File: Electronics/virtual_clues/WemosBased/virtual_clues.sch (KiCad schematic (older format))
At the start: 22 parts, among them Q1 IRLB8721PBF, U1 L7805

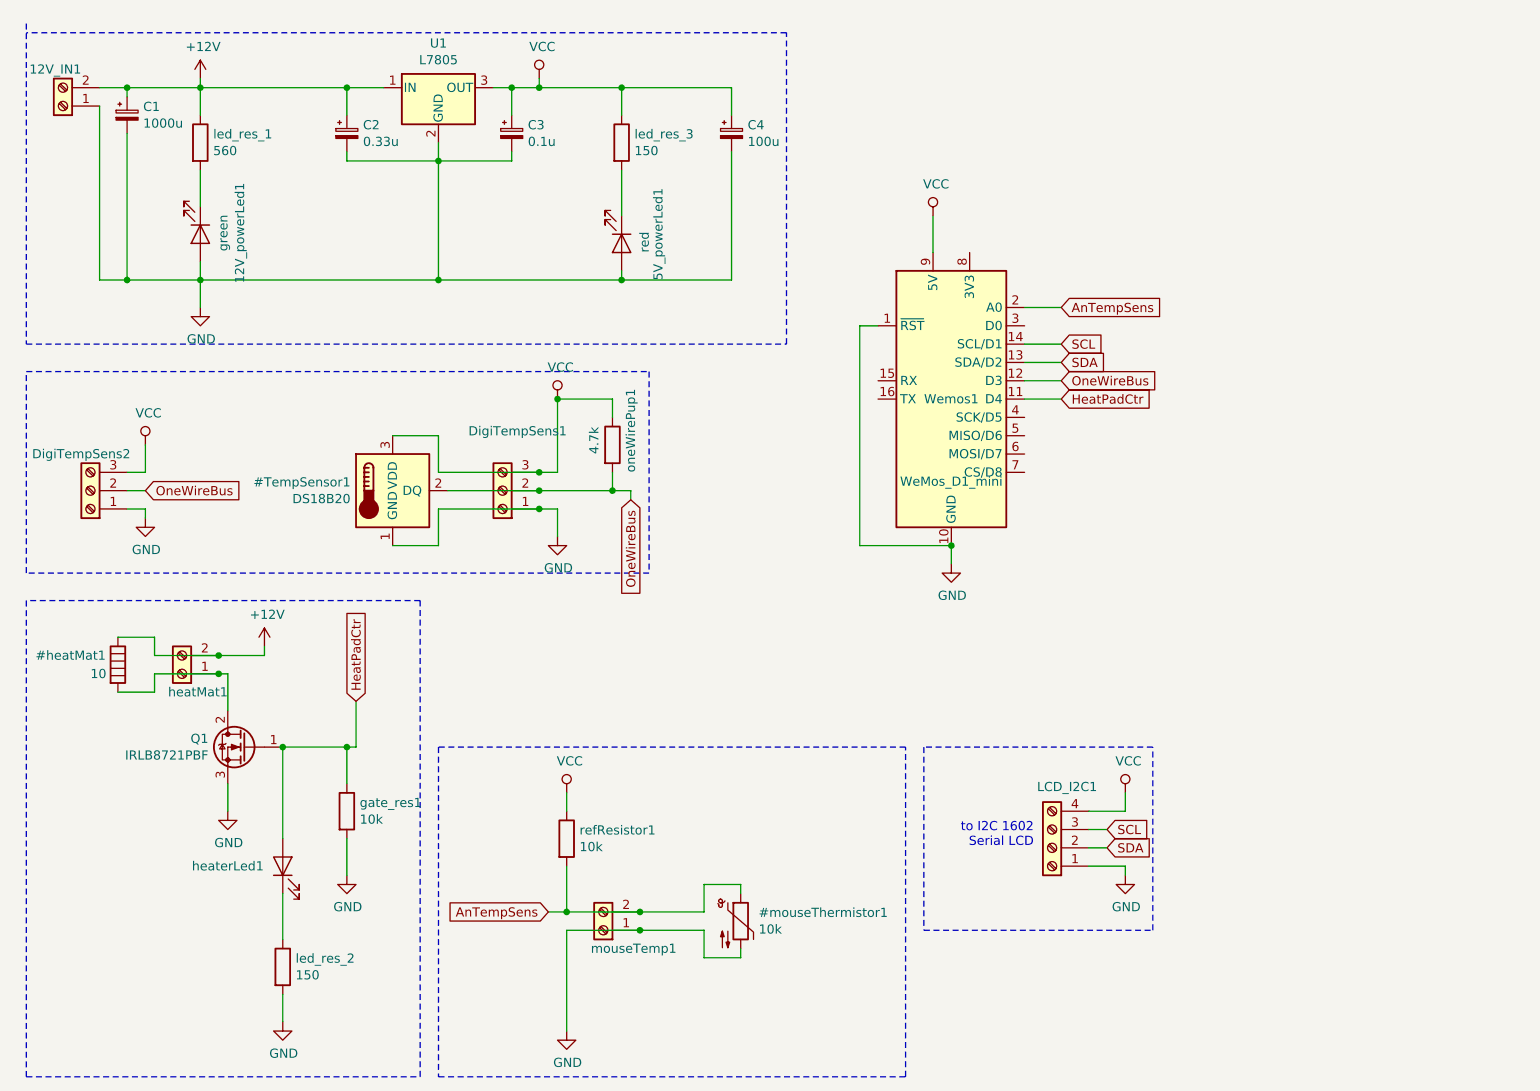
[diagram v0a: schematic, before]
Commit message: update PCB for 3rd temp sensor and additional heat pad + better labels
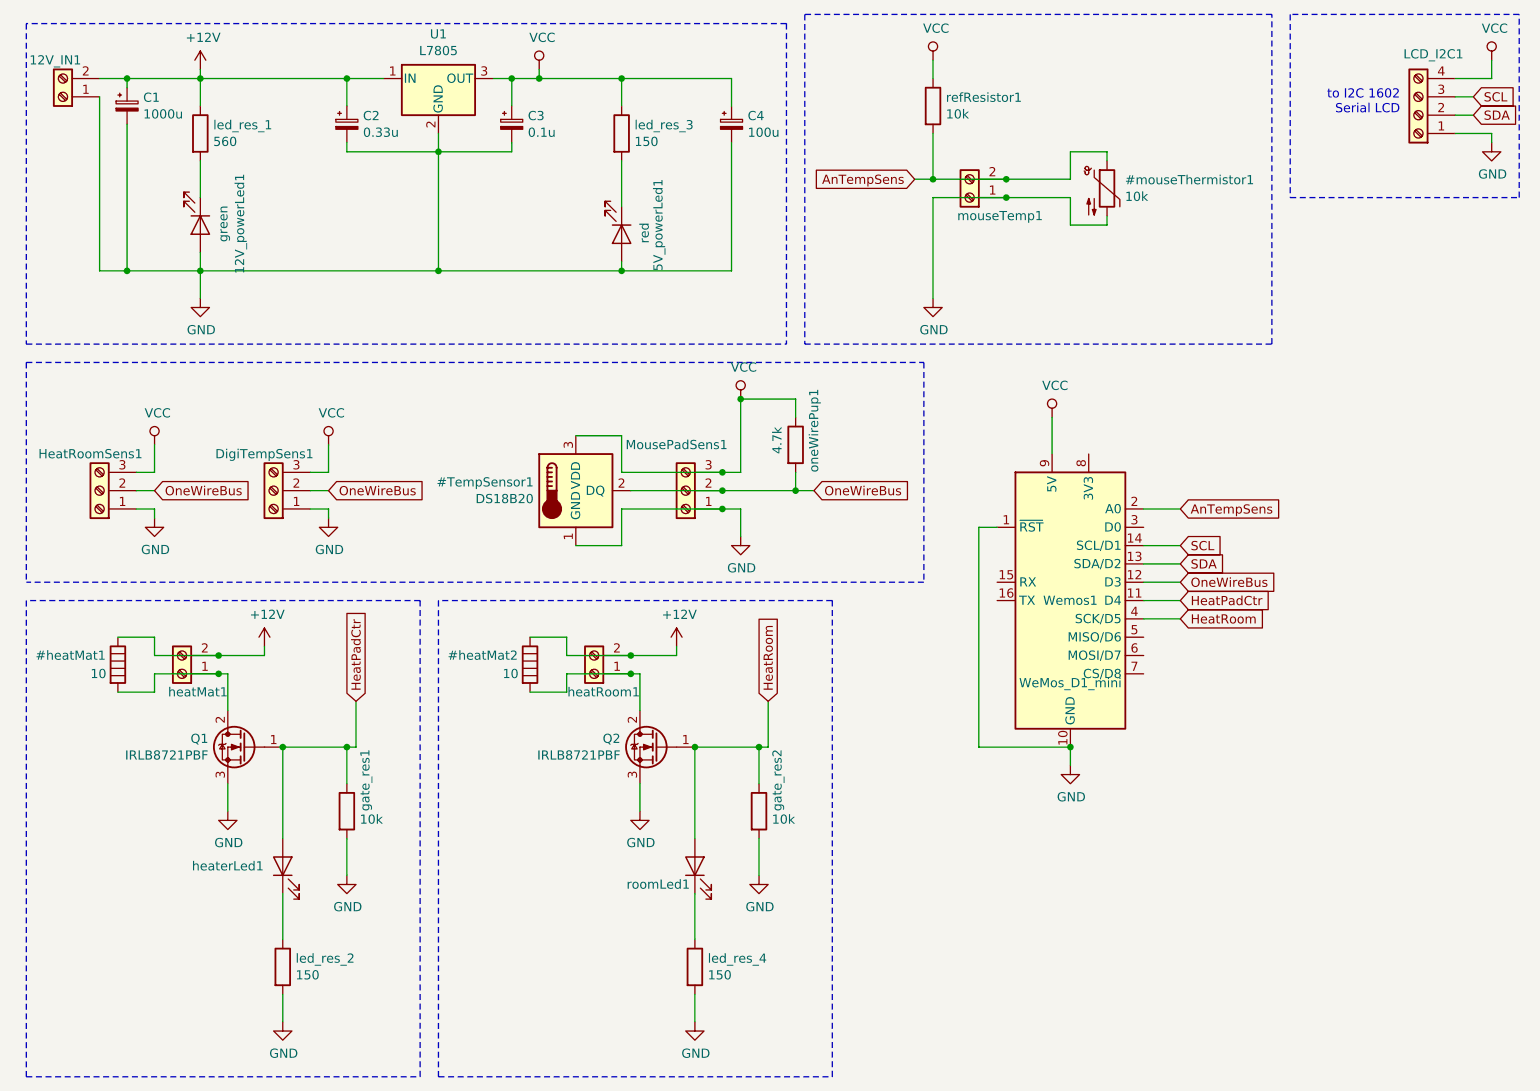
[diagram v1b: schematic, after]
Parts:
- added DigiTempSens1: DigiTempSens2, TerminalBlock_Phoenix:TerminalBlock_Phoenix_MPT-0,5-3-2.54_1x03_P2.54mm_Horizontal, symbol Connector:Screw_Terminal_01x03
- added Q2: IRLB8721PBF, Package_TO_SOT_THT:TO-220-3_Vertical, symbol Transistor_FET:IRLB8721PBF
- added gate_res2: 10k, Resistor_THT:R_Axial_DIN0207_L6.3mm_D2.5mm_P10.16mm_Horizontal, symbol Device:R
- added heatRoom1: heatMat1, TerminalBlock_MetzConnect:TerminalBlock_MetzConnect_Type094_RT03502HBLU_1x02_P5.00mm_Horizontal, symbol Connector:Screw_Terminal_01x02
- added led_res_4: 150, Resistor_THT:R_Axial_DIN0207_L6.3mm_D2.5mm_P10.16mm_Horizontal, symbol Device:R
- added roomLed1: heaterLed, LED_THT:LED_D5.0mm_Horizontal_O6.35mm_Z3.0mm, symbol Device:LED
- renumbered DigiTempSens2 to HeatRoomSens1, DigiTempSens1 to MousePadSens1
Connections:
- net +12V: now also heatRoom1.2 (Pin_2)
- net GND: now also DigiTempSens1.1 (Pin_1), Q2.3 (S), gate_res2.2, led_res_4.2
- net OneWireBus: now also DigiTempSens1.2 (Pin_2)
- net VCC: now also DigiTempSens1.3 (Pin_3)
- net HeatRoom: now reaches Wemos1.4 (SCK/D5)
- net HeatRoom: now also Q2.1 (G), gate_res2.1, roomLed1.2 (A)
- new net: led_res_4.1, roomLed1.1 (K)
- new net: Q2.2 (D), heatRoom1.1 (Pin_1)
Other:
- moved on the sheet: 12V_IN1, 12V_powerLed1, 5V_powerLed1, C1, C2, C3, C4, HeatRoomSens1, LCD_I2C1, MousePadSens1, U1, Wemos1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
